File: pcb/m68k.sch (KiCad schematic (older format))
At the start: 120 parts, among them J1 USB_B_Micro, J2 Mini-DIN-6, J4 DB15_Male_HighDensity, J5 FTSH-105-01-L-DV-K, J6 FTSH-105-01-L-DV-K, J7 FTSH-105-01-L-DV-K, J8 Micro_SD_Card, U1 93LC56, U10 25LCxxx, U11 TXB0108DQSR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

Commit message: Home
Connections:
- net CDONE: now also U12.1 (A1); no longer U12.2 (A2)
- net HALTn: now also U12.18 (B2); no longer U12.20 (B1)
- net RESETn: now also U12.20 (B1); no longer U12.18 (B2)
- net at U13.60 (IOB_95): now also U12.2 (A2); no longer U12.1 (A1)
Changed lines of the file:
@@
 Connection ~ 1550 14950
 Wire Wire Line
-	7050 8250 6950 8250
+	7050 8150 6950 8150
 Wire Wire Line
 	6950 7000 7050 7000
@@
 	1    0    0    -1
 $EndComp
-Text GLabel 6950 8250 0    50   BiDi ~ 0
+Text GLabel 6950 8150 0    50   BiDi ~ 0
 RESETn
-Text GLabel 8300 8250 2    50   Input ~ 0
+Text GLabel 8300 8150 2    50   Input ~ 0
 CDONE
 $Comp
@@
 Wire Wire Line
 	3400 8950 3500 8950
-Text GLabel 6950 8150 0    50   BiDi ~ 0
+Text GLabel 6950 8250 0    50   BiDi ~ 0
 HALTn
 Wire Wire Line
@@
 NoConn ~ 7050 8850
 Wire Wire Line
-	6950 8150 7050 8150
+	6950 8250 7050 8250
 Wire Wire Line
 	6550 8350 7050 8350
@@
 	7850 8350 8300 8350
 Wire Wire Line
-	7850 8250 8300 8250
-Wire Wire Line
-	7850 8150 8750 8150
+	7850 8150 8300 8150
 Wire Wire Line
-	8750 8150 8750 10300
+	7850 8250 8750 8250
 Wire Wire Line
 	8750 10300 12150 10300
@@
 Wire Wire Line
 	12150 9750 13100 9750
+Wire Wire Line
+	8750 8250 8750 10300
 Wire Bus Line
 	18600 2100 18600 2800

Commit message: I finally broke something
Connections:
- net ASn: now also U12.12 (B8); no longer U11.13 (B7)
- net BGn: now also U11.13 (B7); no longer U11.16 (B4)
- net E: now also U12.13 (B7); no longer U11.14 (B6)
- net FC0: now also U11.16 (B4); no longer U11.20 (B1)
- net FC1: now also U11.15 (B5); no longer U11.18 (B2)
- net FC2: now also U11.14 (B6); no longer U11.17 (B3)
- net LDSn: now also U11.17 (B3); no longer U12.13 (B7)
- net R_Wn: now also U11.20 (B1); no longer U12.15 (B5)
- net UDSn: now also U11.18 (B2); no longer U12.14 (B6)
- net VMAn: now also U11.12 (B8); no longer U11.15 (B5)
- net at U13.136 (IOT_214): now also U12.9 (A7); no longer U11.1 (A1)
- net at U13.137 (IOT_215): now also U12.10 (A8); no longer U11.2 (A2)
- net at U13.138 (IOT_216): now also U11.4 (A4); no longer U11.3 (A3)
- net at U13.139 (IOT_217): now also U11.7 (A5); no longer U11.4 (A4)
- net at U13.141 (IOT_219): now also U11.8 (A6); no longer U11.7 (A5)
- net at U13.142 (IOT_220): now also U11.9 (A7); no longer U11.8 (A6)
- net at U13.143 (IOT_221): now also U11.10 (A8); no longer U11.9 (A7)
- net at U13.15 (IOL_10A), U9.11 (WE#): now also U11.1 (A1); no longer U12.7 (A5)
- net at U13.16 (IOL_10B), U9.14 (UB#): now also U11.2 (A2); no longer U12.8 (A6)
- net at U13.17 (IOL_12A), U9.15 (LB#): now also U11.3 (A3); no longer U12.9 (A7)
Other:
- moved on the sheet: J2, R13, R14, U11, U12

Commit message: Fin
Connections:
- net BGn: now also U11.16 (B4); no longer U11.13 (B7)
- net FC0: now also U11.12 (B8); no longer U11.16 (B4)
- net FC1: now also U11.13 (B7); no longer U11.15 (B5)
- net VMAn: now also U11.15 (B5); no longer U11.12 (B8)
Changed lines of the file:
@@
 Connection ~ 1550 14950
 Wire Wire Line
-	6950 7100 6850 7100
-Wire Wire Line
-	6850 7000 6950 7000
+	6950 6800 6850 6800
+Wire Wire Line
+	6850 6700 6950 6700
 Text GLabel 12900 8950 0    50   Output ~ 0
 VPAn
-Text GLabel 6850 7100 0    50   Input ~ 0
+Text GLabel 6850 6800 0    50   Input ~ 0
 VMAn
 Text GLabel 12900 8850 0    50   Output ~ 0
 BRn
-Text GLabel 6850 7000 0    50   Input ~ 0
+Text GLabel 6850 6700 0    50   Input ~ 0
 BGn
 Text GLabel 12900 8750 0    50   Output ~ 0
@@
 	6850 6900 6950 6900
 Wire Wire Line
-	6950 6800 6850 6800
+	6950 7000 6850 7000
 Text GLabel 12900 8650 0    50   Output ~ 0
 IPL2n
@@
 IPL0n
 Wire Wire Line
-	6950 6700 6850 6700
+	6950 7100 6850 7100
 Text GLabel 12900 8350 0    50   Output ~ 0
 DTACKn
@@
 Wire Wire Line
 	14100 4000 13850 4000
-Text GLabel 6850 6700 0    50   Input ~ 0
+Text GLabel 6850 7100 0    50   Input ~ 0
 FC0
-Text GLabel 6850 6800 0    50   Input ~ 0
+Text GLabel 6850 7000 0    50   Input ~ 0
 FC1
 Text GLabel 6850 6900 0    50   Input ~ 0

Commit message: almost finish routing
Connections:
- net +3V3: now also R8.1; no longer R8.2
- net CDONE: now also U3.23 (ADBUS6); no longer U3.24 (ADBUS7)
- net CRESET_Bn: now also U3.24 (ADBUS7); no longer U3.23 (ADBUS6)
- net nHOLD: now also U13.64 (IOB_104_CBSEL1); no longer U13.70 (IOB_107_SCK)
- net at R10.1, U10.1 (~CS), U3.21 (ADBUS4): now also U13.71 (IOB_108_SS); no longer U13.67 (IOB_105_SDO)
- net at U10.5 (MOSI), U3.17 (ADBUS1): now also U13.67 (IOB_105_SDO); no longer U13.68 (IOB_106_SDI)
- net at U10.6 (SCK), U3.16 (ADBUS0): now also R8.2, U13.70 (IOB_107_SCK); no longer R8.1, U13.71 (IOB_108_SS)
- net ADBUS: no longer names the net of U10.2 (MISO), U3.18 (ADBUS2)
- net ADBUS: now also U13.68 (IOB_106_SDI); no longer U13.64 (IOB_104_CBSEL1)
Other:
- moved on the sheet: R10, R11, R12, R8
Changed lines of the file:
@@
 Wire Wire Line
 	7200 3500 8050 3500
-Text GLabel 5450 12500 2    50   Input ~ 0
+Text GLabel 5450 12400 2    50   Input ~ 0
 CDONE
 Wire Wire Line
@@
 Wire Wire Line
 	8400 6300 8400 6350
-Text GLabel 13000 10150 0    50   Input ~ 0
-ADBUS
 Wire Wire Line
 	11300 9150 11850 9150
@@
 Wire Wire Line
 	8550 6400 8500 6400
-Wire Wire Line
-	6650 12300 6650 11800
-Text GLabel 6200 12000 2    50   Input ~ 0
-ADBUS
 $Comp
 L Memory_EEPROM:25LCxxx U10
@@
 	1    0    0    -1
 $EndComp
-Text GLabel 5450 12400 2    50   Output ~ 0
+Text GLabel 5450 12500 2    50   Output ~ 0
 CRESET_Bn
 Text GLabel 8300 12300 2    50   BiDi ~ 0
 nWP
-Wire Wire Line
-	7300 12100 7300 11600
-Text GLabel 8750 11800 0    50   BiDi ~ 0
+Text GLabel 13000 10150 0    50   BiDi ~ 0
 nHOLD
 $Comp
 L Device:R R12
 U 1 1 62339B13
-P 8150 12100
-F 0 "R12" V 8200 12000 50  0000 R CNN
-F 1 "10k" V 8150 12200 50  0000 R CNN
-F 2 "Resistor_SMD:R_0603_1608Metric" V 8080 12100 50  0001 C CNN
-F 3 "~" H 8150 12100 50  0001 C CNN
-	1    8150 12100
+P 8150 11450
+F 0 "R12" V 8200 11350 50  0000 R CNN
+F 1 "10k" V 8150 11550 50  0000 R CNN
+F 2 "Resistor_SMD:R_0603_1608Metric" V 8080 11450 50  0001 C CNN
+F 3 "~" H 8150 11450 50  0001 C CNN
+	1    8150 11450
 	-1   0    0    1
 $EndComp
@@
 L Device:R R11
 U 1 1 6233983C
-P 7950 12100
-F 0 "R11" V 8000 12000 50  0000 R CNN
-F 1 "10k" V 7950 12200 50  0000 R CNN
-F 2 "Resistor_SMD:R_0603_1608Metric" V 7880 12100 50  0001 C CNN
-F 3 "~" H 7950 12100 50  0001 C CNN
-	1    7950 12100
+P 7950 11450
+F 0 "R11" V 8000 11350 50  0000 R CNN
+F 1 "10k" V 7950 11550 50  0000 R CNN
+F 2 "Resistor_SMD:R_0603_1608Metric" V 7880 11450 50  0001 C CNN
+F 3 "~" H 7950 11450 50  0001 C CNN
+	1    7950 11450
 	-1   0    0    1
 $EndComp
@@
 L power:+3V3 #PWR0125
 U 1 1 605A3C62
-P 7300 11600
-F 0 "#PWR0125" H 7300 11450 50  0001 C CNN
-F 1 "+3V3" H 7315 11773 50  0000 C CNN
-F 2 "" H 7300 11600 50  0001 C CNN
-F 3 "" H 7300 11600 50  0001 C CNN
-	1    7300 11600
+P 7300 11300
+F 0 "#PWR0125" H 7300 11150 50  0001 C CNN
+F 1 "+3V3" H 7315 11473 50  0000 C CNN
+F 2 "" H 7300 11300 50  0001 C CNN
+F 3 "" H 7300 11300 50  0001 C CNN
+	1    7300 11300
 	1    0    0    -1
 $EndComp
@@
 L Device:R R8
 U 1 1 605A381A
-P 6800 12100
-F 0 "R8" V 6850 12000 50  0000 R CNN
-F 1 "10k" V 6800 12200 50  0000 R CNN
-F 2 "Resistor_SMD:R_0603_1608Metric" V 6730 12100 50  0001 C CNN
-F 3 "~" H 6800 12100 50  0001 C CNN
-	1    6800 12100
-	-1   0    0    1
+P 6750 11450
+F 0 "R8" V 6800 11350 50  0000 R CNN
+F 1 "10k" V 6750 11550 50  0000 R CNN
+F 2 "Resistor_SMD:R_0603_1608Metric" V 6680 11450 50  0001 C CNN
+F 3 "~" H 6750 11450 50  0001 C CNN
+	1    6750 11450
+	1    0    0    -1
 $EndComp
 $Comp
 L Device:R R10
 U 1 1 605A28F2
-P 7750 12100
-F 0 "R10" V 7800 12000 50  0000 R CNN
-F 1 "10k" V 7750 12200 50  0000 R CNN
-F 2 "Resistor_SMD:R_0603_1608Metric" V 7680 12100 50  0001 C CNN
-F 3 "~" H 7750 12100 50  0001 C CNN
-	1    7750 12100
+P 7750 11450
+F 0 "R10" V 7800 11350 50  0000 R CNN
+F 1 "10k" V 7750 11550 50  0000 R CNN
+F 2 "Resistor_SMD:R_0603_1608Metric" V 7680 11450 50  0001 C CNN
+F 3 "~" H 7750 11450 50  0001 C CNN
+	1    7750 11450
 	-1   0    0    1
 $EndComp
 Wire Wire Line
-	6550 11900 6550 12400
-Wire Wire Line
 	7700 12300 8150 12300
 Wire Wire Line
 	7700 12400 7950 12400
 Wire Wire Line
-	8150 11950 8150 11600
-Wire Wire Line
-	7950 11950 7950 11600
-Wire Wire Line
-	7950 11600 8150 11600
-Connection ~ 8150 11600
-Wire Wire Line
-	7750 11950 7750 11600
-Wire Wire Line
-	7750 11600 7950 11600
-Connection ~ 7950 11600
-Wire Wire Line
-	7750 12250 7750 12500
-Wire Wire Line
-	7950 12250 7950 12400
-Wire Wire Line
-	6100 12000 6100 12500
-Connection ~ 6100 12000
-Wire Wire Line
-	6100 12000 6200 12000
-Wire Wire Line
 	5350 12200 6000 12200
-Wire Wire Line
-	5350 12000 6100 12000
-Wire Wire Line
-	6000 12200 6000 12950
-Wire Wire Line
-	7750 12500 7750 12950
-Connection ~ 7750 12500
 Connection ~ 7950 12400
 Text GLabel 8300 12400 2    50   BiDi ~ 0
@@
 Wire Wire Line
 	7950 12400 8300 12400
-Wire Wire Line
-	8150 12250 8150 12300
 Connection ~ 8150 12300
 Wire Wire Line
 	8150 12300 8300 12300
 Wire Wire Line
-	8650 12000 8650 12950
-Connection ~ 7750 11600
-Connection ~ 7300 11600
-Connection ~ 7750 12950
-Wire Wire Line
-	6000 12950 7750 12950
-Connection ~ 6550 11900
-Wire Wire Line
-	6800 11950 6800 11600
-Wire Wire Line
-	6800 11600 7300 11600
-Wire Wire Line
-	8350 11800 8350 11700
-Connection ~ 6650 11800
-Wire Wire Line
-	6800 12250 6800 12300
-Wire Wire Line
-	6800 12300 6900 12300
-Wire Wire Line
-	6650 12300 6800 12300
-Connection ~ 6800 12300
-Wire Wire Line
-	6550 12400 6900 12400
-Wire Wire Line
-	6100 12500 6900 12500
-Wire Wire Line
-	7750 12950 8650 12950
-Wire Wire Line
-	8650 12000 8750 12000
-Wire Wire Line
-	8150 11600 8750 11600
-Wire Wire Line
-	6550 11900 8750 11900
-Wire Wire Line
-	5350 11800 6650 11800
-Wire Wire Line
-	7300 11600 7750 11600
-Wire Wire Line
-	5350 11900 6550 11900
-Wire Wire Line
-	8350 11700 8750 11700
-Wire Wire Line
-	6650 11800 8350 11800
-Wire Wire Line
 	12150 10300 12150 9750
 Wire Wire Line
@@
 Wire Wire Line
 	7750 8750 8150 8750
+Wire Wire Line
+	5350 11800 6750 11800
+Wire Wire Line
+	6000 12200 6000 11700
+Wire Wire Line
+	6000 11700 7750 11700
+Wire Wire Line
+	5350 12000 6100 12000
+Wire Wire Line
+	5350 11900 6100 11900
+Wire Wire Line
+	6100 11900 6200 12000
+Wire Wire Line
+	6100 12000 6200 11900
+Wire Wire Line
+	6200 11900 6550 11900
+Wire Wire Line
+	6200 12000 6650 12000
+Wire Wire Line
+	6900 12300 6750 12300
+Wire Wire Line
+	6750 12300 6750 11800
+Connection ~ 6750 11800
+Wire Wire Line
+	6750 11800 8750 11800
+Wire Wire Line
+	6900 12400 6650 12400
+Wire Wire Line
+	6650 12400 6650 12000
+Connection ~ 6650 12000
+Wire Wire Line
+	6650 12000 8750 12000
+Wire Wire Line
+	6900 12500 6550 12500
+Wire Wire Line
+	6550 12500 6550 11900
+Connection ~ 6550 11900
+Wire Wire Line
+	6550 11900 8750 11900
+Wire Wire Line
+	7750 11700 7750 12500
+Connection ~ 7750 11700
+Wire Wire Line
+	7750 11700 8750 11700
+Connection ~ 7750 11300
+Connection ~ 7950 11300
+Connection ~ 8150 11300
+Wire Wire Line
+	8150 11300 8700 11300
+Wire Wire Line
+	7750 11300 7950 11300
+Wire Wire Line
+	7950 11300 8150 11300
+Wire Wire Line
+	7950 11600 7950 12400
+Wire Wire Line
+	7750 11700 7750 11600
+Wire Wire Line
+	8150 11600 8150 12300
+Wire Wire Line
+	6750 11800 6750 11600
+Wire Wire Line
+	8700 11300 8700 11600
+Wire Wire Line
+	8700 11600 8750 11600
+Wire Wire Line
+	7300 12100 7300 11300
+Connection ~ 7300 11300
+Wire Wire Line
+	7300 11300 7750 11300
+Wire Wire Line
+	6750 11300 7300 11300
 Wire Bus Line
 	18600 2100 18600 2800

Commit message: vanity
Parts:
- added H1, H2, H3: MountingHole_Pad, MountingHole:MountingHole_2.5mm_Pad, symbol Mechanical:MountingHole_Pad
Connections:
- net GND: now also H1.1, H2.1, H3.1
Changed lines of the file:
@@
 Wire Wire Line
 	6750 11300 7300 11300
+Wire Wire Line
+	15150 6800 15150 7000
+Connection ~ 15150 7000
+Wire Wire Line
+	15150 7000 15150 7200
+Connection ~ 15150 7200
+Wire Wire Line
+	15150 7200 15150 7350
+$Comp
+L power:GND #PWR06
+U 1 1 5EA04520
+P 15150 7350
+F 0 "#PWR06" H 15150 7100 50  0001 C CNN
+F 1 "GND" H 15155 7177 50  0000 C CNN
+F 2 "" H 15150 7350 50  0001 C CNN
+F 3 "" H 15150 7350 50  0001 C CNN
+	1    15150 7350
+	1    0    0    -1
+$EndComp
+$Comp
+L Mechanical:MountingHole_Pad H1
+U 1 1 5EA6048F
+P 15050 6800
+F 0 "H1" V 15287 6803 50  0000 C CNN
+F 1 "MountingHole_Pad" V 15196 6803 50  0000 C CNN
+F 2 "MountingHole:MountingHole_2.5mm_Pad" H 15050 6800 50  0001 C CNN
+F 3 "~" H 15050 6800 50  0001 C CNN
+	1    15050 6800
+	0    -1   -1   0
+$EndComp
+$Comp
+L Mechanical:MountingHole_Pad H2
+U 1 1 5EA61D1E
+P 15050 7000
+F 0 "H2" V 15287 7003 50  0000 C CNN
+F 1 "MountingHole_Pad" V 15196 7003 50  0000 C CNN
+F 2 "MountingHole:MountingHole_2.5mm_Pad" H 15050 7000 50  0001 C CNN
+F 3 "~" H 15050 7000 50  0001 C CNN
+	1    15050 7000
+	0    -1   -1   0
+$EndComp
+$Comp
+L Mechanical:MountingHole_Pad H3
+U 1 1 5EA63D7B
+P 15050 7200
+F 0 "H3" V 15287 7203 50  0000 C CNN
+F 1 "MountingHole_Pad" V 15196 7203 50  0000 C CNN
+F 2 "MountingHole:MountingHole_2.5mm_Pad" H 15050 7200 50  0001 C CNN
+F 3 "~" H 15050 7200 50  0001 C CNN
+	1    15050 7200
+	0    -1   -1   0
+$EndComp
 Wire Bus Line
 	18600 2100 18600 2800

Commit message: pre pour
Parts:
- removed C25, C26: 10uF, Capacitor_SMD:C_0603_1608Metric, symbol Device:C
- removed C28, C29: 1uF, Capacitor_SMD:C_0603_1608Metric, symbol Device:C
- removed C31, C32, C35, C39: 0.1uF, Capacitor_SMD:C_0603_1608Metric, symbol Device:C
- removed C57, C59, C61: 0.01uF, Capacitor_SMD:C_0603_1608Metric, symbol Device:C
- removed J5, J6, J7: FTSH-105-01-L-DV-K, Connector_PinHeader_2.54mm:PinHeader_2x05_P2.54mm_Vertical, symbol m68k-rescue:FTSH-105-01-L-DV-K-dk_Rectangular-Connectors-Headers-Male-Pins
- added H4: MountingHole_Pad, MountingHole:MountingHole_2.2mm_M2_Pad, symbol Mechanical:MountingHole_Pad
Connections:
- net GND: now also H4.1
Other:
- moved on the sheet: C34, C38, C41, C42, C43, C46, C47, C49, C51, C53, C55

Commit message: update ps/2, usb, and mounting hole.
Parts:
- H4: footprint MountingHole:MountingHole_2.2mm_M2_Pad -> MountingHole:MountingHole_2.5mm_Pad
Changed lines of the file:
@@
 F 0 "H4" V 15287 6603 50  0000 C CNN
 F 1 "MountingHole_Pad" V 15196 6603 50  0000 C CNN
-F 2 "MountingHole:MountingHole_2.2mm_M2_Pad" H 15050 6600 50  0001 C CNN
+F 2 "MountingHole:MountingHole_2.5mm_Pad" H 15050 6600 50  0001 C CNN
 F 3 "~" H 15050 6600 50  0001 C CNN
 	1    15050 6600

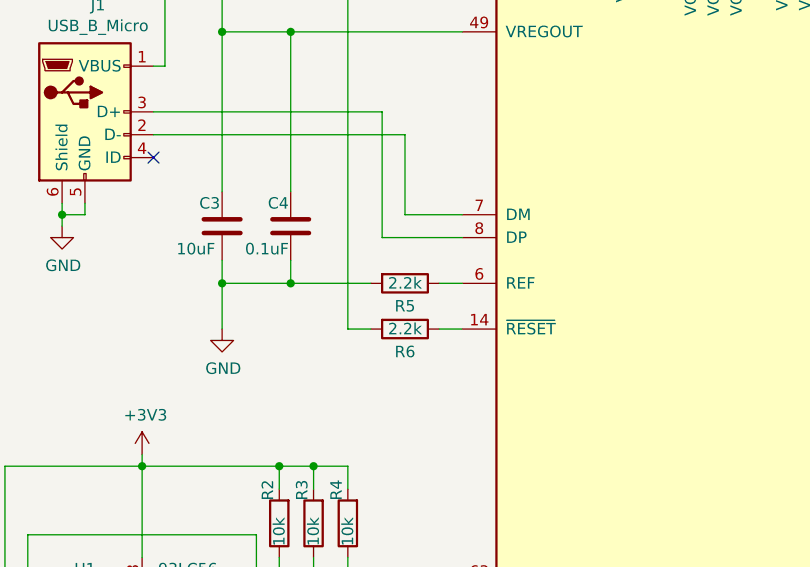
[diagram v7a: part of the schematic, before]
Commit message: update resistor value
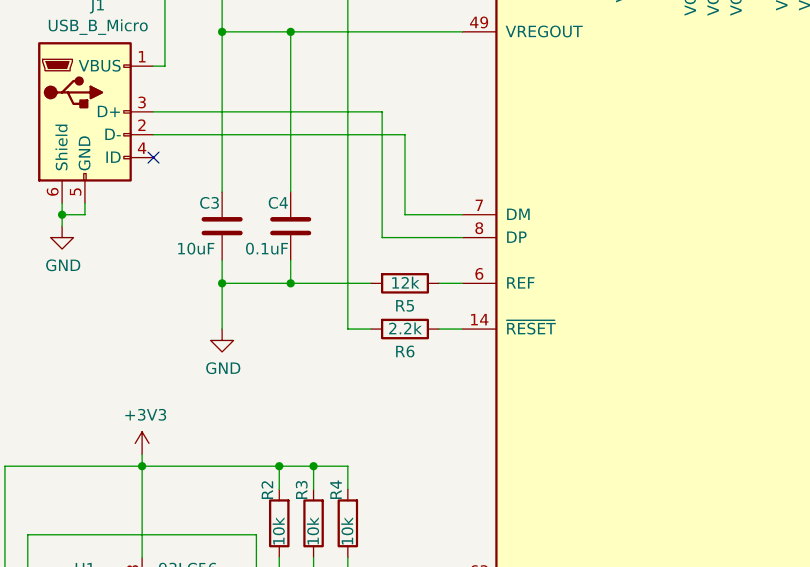
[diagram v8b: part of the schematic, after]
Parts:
- R5: value 2.2k -> 12k
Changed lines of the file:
@@
 P 2700 13100
 F 0 "R5" V 2800 13100 50  0000 C CNN
-F 1 "2.2k" V 2700 13100 50  0000 C CNN
+F 1 "12k" V 2700 13100 50  0000 C CNN
 F 2 "Resistor_SMD:R_0603_1608Metric" V 2630 13100 50  0001 C CNN
 F 3 "~" H 2700 13100 50  0001 C CNN
